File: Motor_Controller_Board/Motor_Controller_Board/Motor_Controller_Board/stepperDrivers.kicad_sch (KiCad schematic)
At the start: 55 parts, among them J401 Conn_01x04, J402 Conn_01x04, J403 Conn_01x04, U401 A4988, U402 A4988, U403 A4988

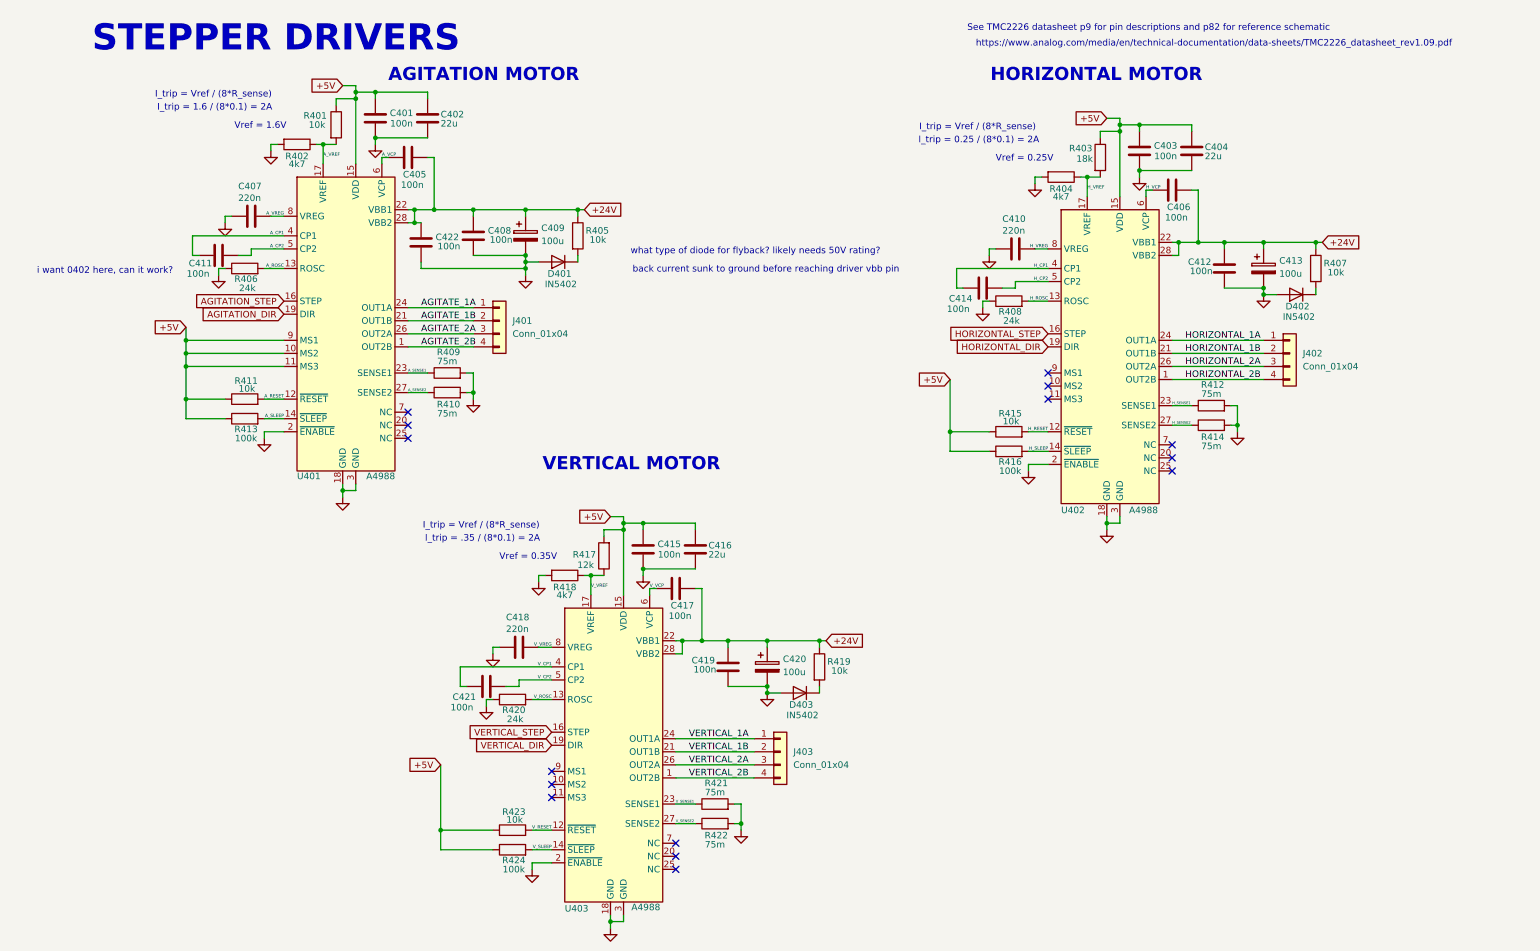
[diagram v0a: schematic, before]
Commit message: discussed with Alex and Mishari. confident in schematic, going to do layout tomorrow
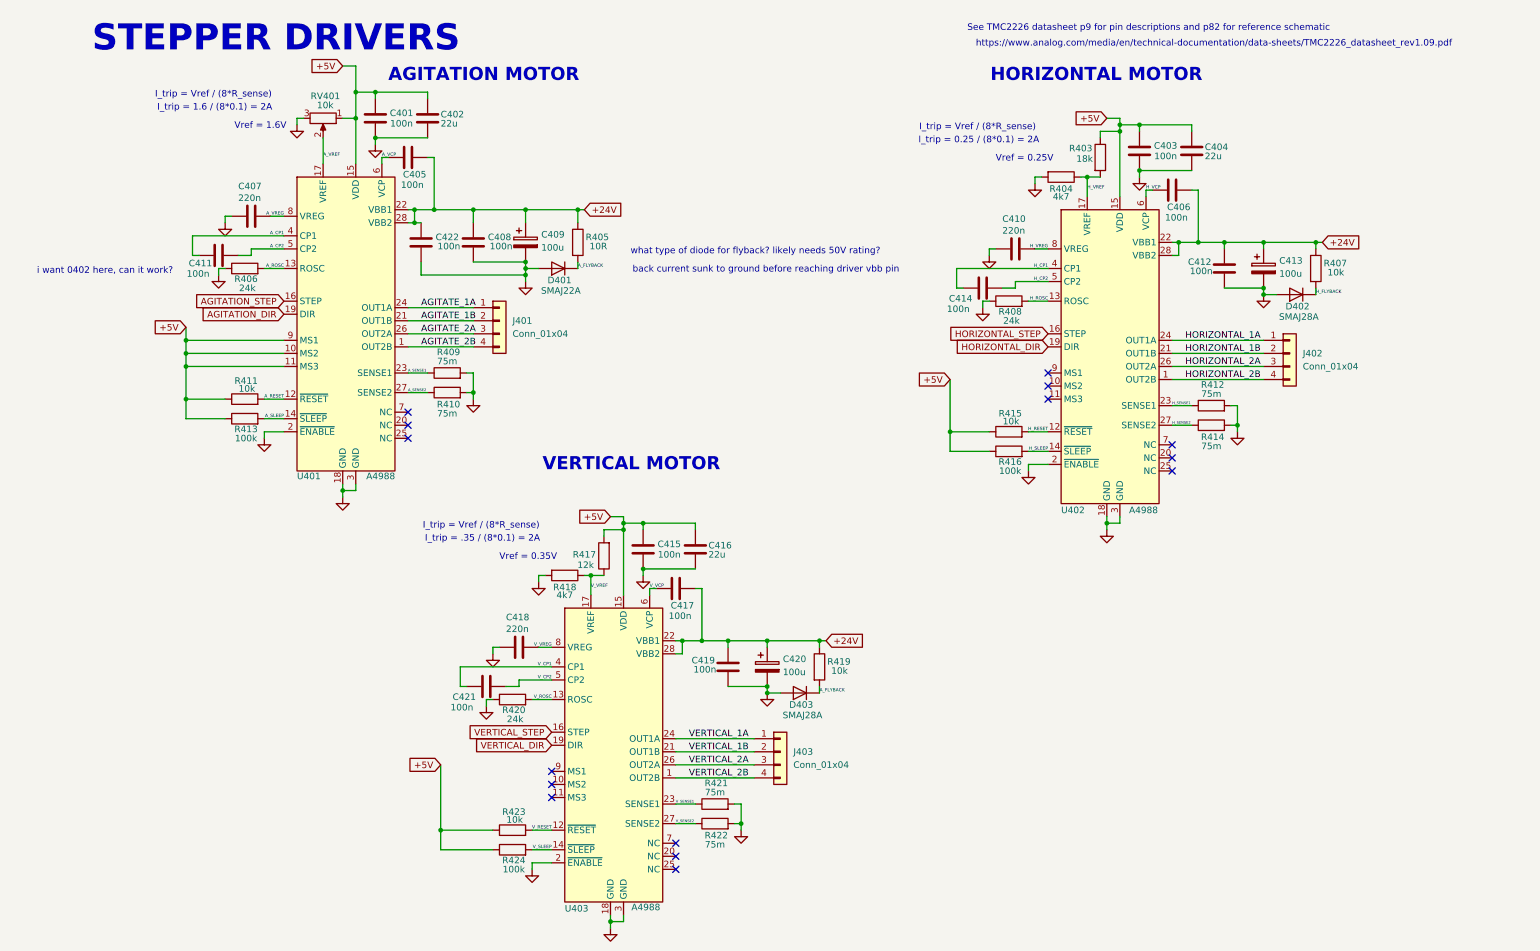
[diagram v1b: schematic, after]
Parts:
- removed R401: 10k, Resistor_SMD:R_0603_1608Metric, symbol Device:R
- removed R402: 4k7, Resistor_SMD:R_0603_1608Metric, symbol Device:R
- added RV401: 10k, symbol Device:R_Potentiometer
- C409, C413, C420: footprint Capacitor_THT:CP_Radial_D16.0mm_P7.50mm -> Capacitor_SMD:CP_Elec_6.3x7.7; LCSC Part Number (none) -> C3339; MPN (none) -> RVT1V101M0607; Manufacturer (none) -> Honor Elec; now in the parts list
- D401: value IN5402 -> SMAJ22A; footprint Diode_THT:D_DO-27_P15.24mm_Horizontal -> Diode_SMD:D_SMA; LCSC Part Number (none) -> C148220; MPN (none) -> SMAJ22A; Manufacturer (none) -> Littelfuse; now in the parts list
- D402, D403: value IN5402 -> SMAJ28A; footprint Diode_THT:D_DO-27_P15.24mm_Horizontal -> Diode_SMD:D_SMA; LCSC Part Number (none) -> C148227; MPN (none) -> SMAJ28A; Manufacturer (none) -> Littelfuse
- R405: value 10k -> 10R
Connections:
- net +5V: now also RV401.1
- net A_VREF: now also RV401.2
- net GND: now also RV401.3
- net A_FLYBACK: now reaches D403.1 (K), R419.2
- net A_FLYBACK: now also D401.1 (K), R405.2
- net H_FLYBACK: now reaches D402.1 (K), R407.2
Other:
- moved on the sheet: C408, C409, D401, R405

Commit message: general placement done. discuss with teammates tomorrow
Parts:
- removed C412, C419: 100n, Capacitor_SMD:C_0603_1608Metric, symbol Device:C
- removed C413, C420: 100u, Capacitor_SMD:CP_Elec_6.3x7.7, symbol Device:C_Polarized
- removed RV401: 10k, symbol Device:R_Potentiometer
- added C413, C414, C421, C422: 100n, Capacitor_SMD:C_0603_1608Metric, symbol Device:C
- added C415, C423: 100u, Capacitor_SMD:CP_Elec_6.3x7.7, symbol Device:C_Polarized
- added R401: 10k, Resistor_SMD:R_0603_1608Metric, symbol Device:R
- added R402: 4k7, Resistor_SMD:R_0603_1608Metric, symbol Device:R
- D402, D403: value SMAJ28A -> SMAJ22A; LCSC Part Number C148227 -> C148220; MPN SMAJ28A -> SMAJ22A; now in the parts list
- R407, R419: value 10k -> 10R
- renumbered C422 to C408, C408 to C409, C409 to C410, C410 to C411, C411 to C412, C414 to C416, C415 to C417, C416 to C418, C417 to C419, C418 to C420, C421 to C424
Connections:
- net +24V: now also C413.2, C414.2, C415.1, C421.2, C422.2, C423.1
- net +5V: now also R401.2
- net AGITATE_1A: now also J401.2 (Pin_2); no longer J401.1 (Pin_1)
- net AGITATE_1B: now also J401.1 (Pin_1); no longer J401.2 (Pin_2)
- net A_FLYBACK: no longer D403.1 (K), R419.2
- net A_VREF: now also R401.1, R402.1
- net GND: now also C413.1, C414.1, C415.2, C421.1, C422.1, C423.2, R402.2
- net HORIZONTAL_1A: now also J402.2 (Pin_2); no longer J402.1 (Pin_1)
- net HORIZONTAL_1B: now also J402.1 (Pin_1); no longer J402.2 (Pin_2)
- net VERTICAL_1A: now also J403.2 (Pin_2); no longer J403.1 (Pin_1)
- net VERTICAL_1B: now also J403.1 (Pin_1); no longer J403.2 (Pin_2)
- new net V_FLYBACK: D403.1 (K), R419.2
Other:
- note added: "CHANGE THIS LCSC PART NUMBER"

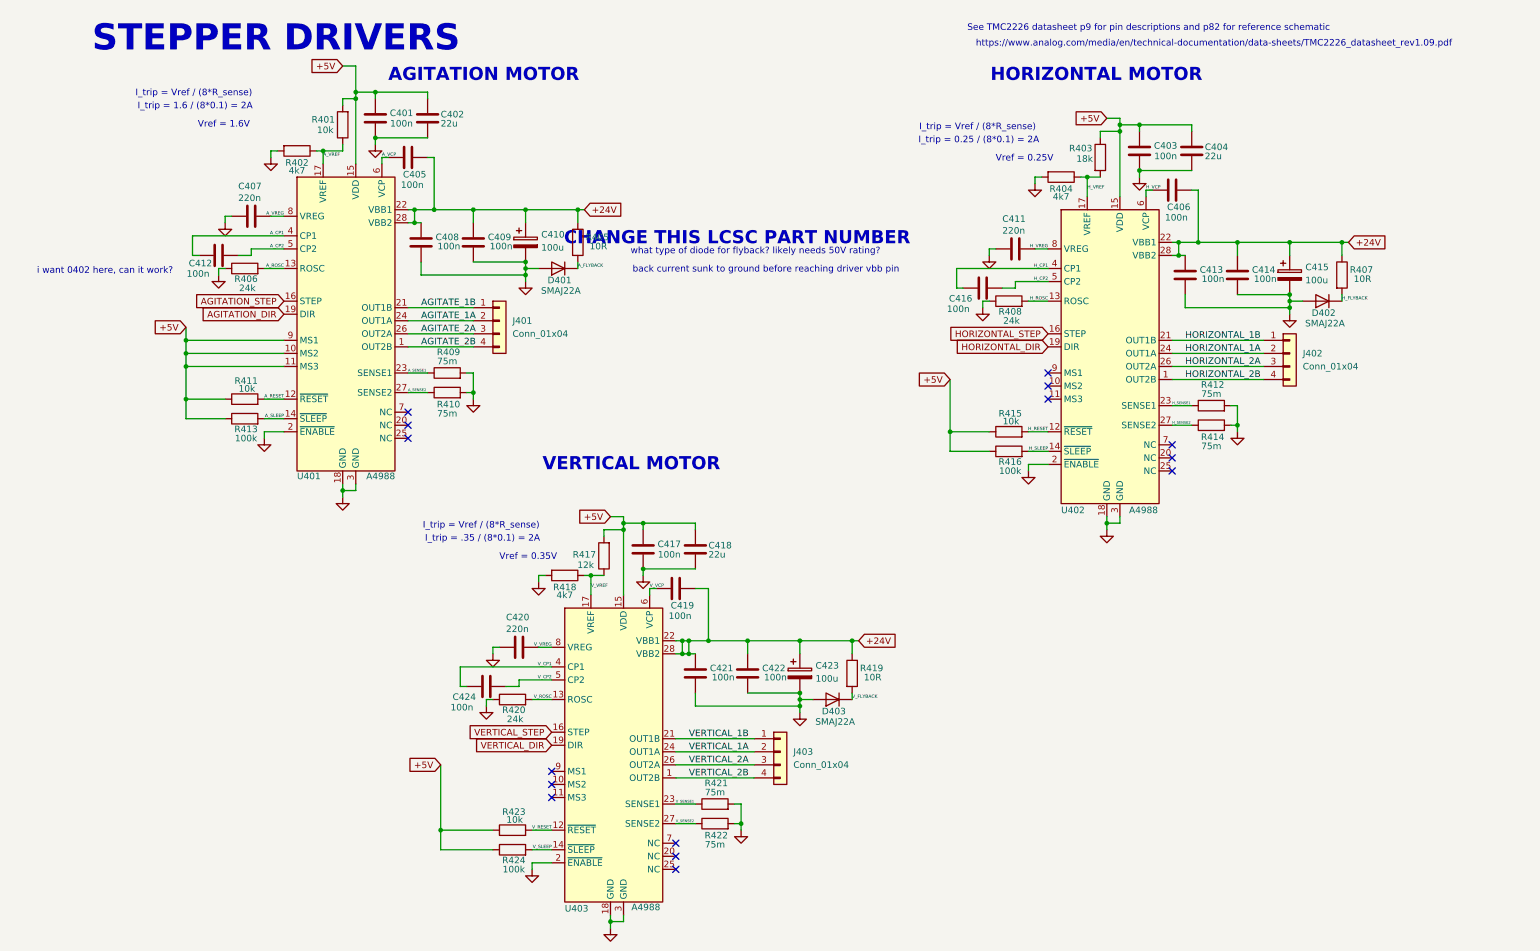
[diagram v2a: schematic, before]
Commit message: routing 75% finished, but very sloppy
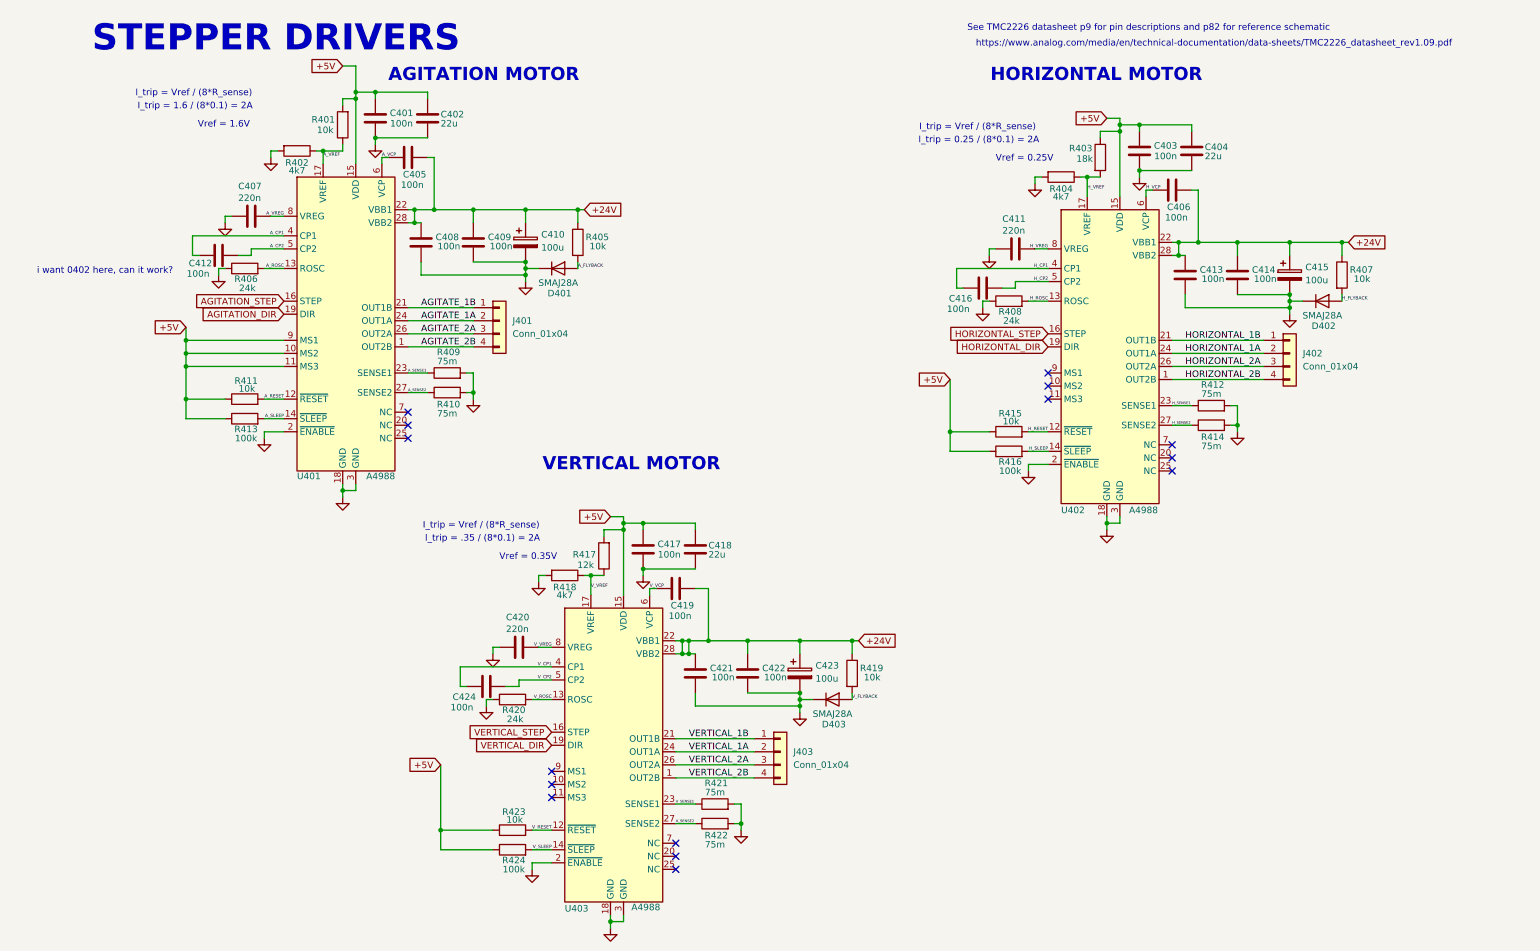
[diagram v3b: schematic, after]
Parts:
- D401, D402, D403: value SMAJ22A -> SMAJ28A; LCSC Part Number C148220 -> C148227; MPN SMAJ22A -> SMAJ28A
- R405, R407, R419: value 10R -> 10k
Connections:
- net A_FLYBACK: now also D401.2 (A); no longer D401.1 (K)
- net GND: now also D401.1 (K), D402.1 (K), D403.1 (K); no longer D401.2 (A), D402.2 (A), D403.2 (A)
- net H_FLYBACK: now also D402.2 (A); no longer D402.1 (K)
- net V_FLYBACK: now also D403.2 (A); no longer D403.1 (K)
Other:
- note removed: "CHANGE THIS LCSC PART NUMBER"
- note removed: "back current sunk to ground before reaching driver vbb pin"
- note removed: "what type of diode for flyback? likely needs 50V rating?"
- moved on the sheet: D401
